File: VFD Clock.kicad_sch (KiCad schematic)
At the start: 27 parts, among them J1 DS3231, U1 74HC595, U10 74HC595, U11 UDN2981A, U12 IV-11 VFD Tube, U13 74HC595, U14 UDN2981A, U15 IV-11 VFD Tube, U16 74HC595, U17 UDN2981A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

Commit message: omg I finally figured out how to link the UDN2981A symbol and footprint I am the goat
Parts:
- added U19: XL6009 Module, Custom Parts:XL6009 Module, symbol Custom Parts:XL6009_Module
- added U20: LM2596 Module, Custom Parts:LM2596 Module, symbol Custom Parts:LM2596_module
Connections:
- net +1.5V: now also U20.3 (Out+)
- net +25V: now also U19.3 (Out+)
- net +5V: now also U19.1 (In+), U20.1 (In+)
- net GND: now also U19.2 (In-), U19.4 (Out-), U20.2 (In-), U20.4 (Out-)

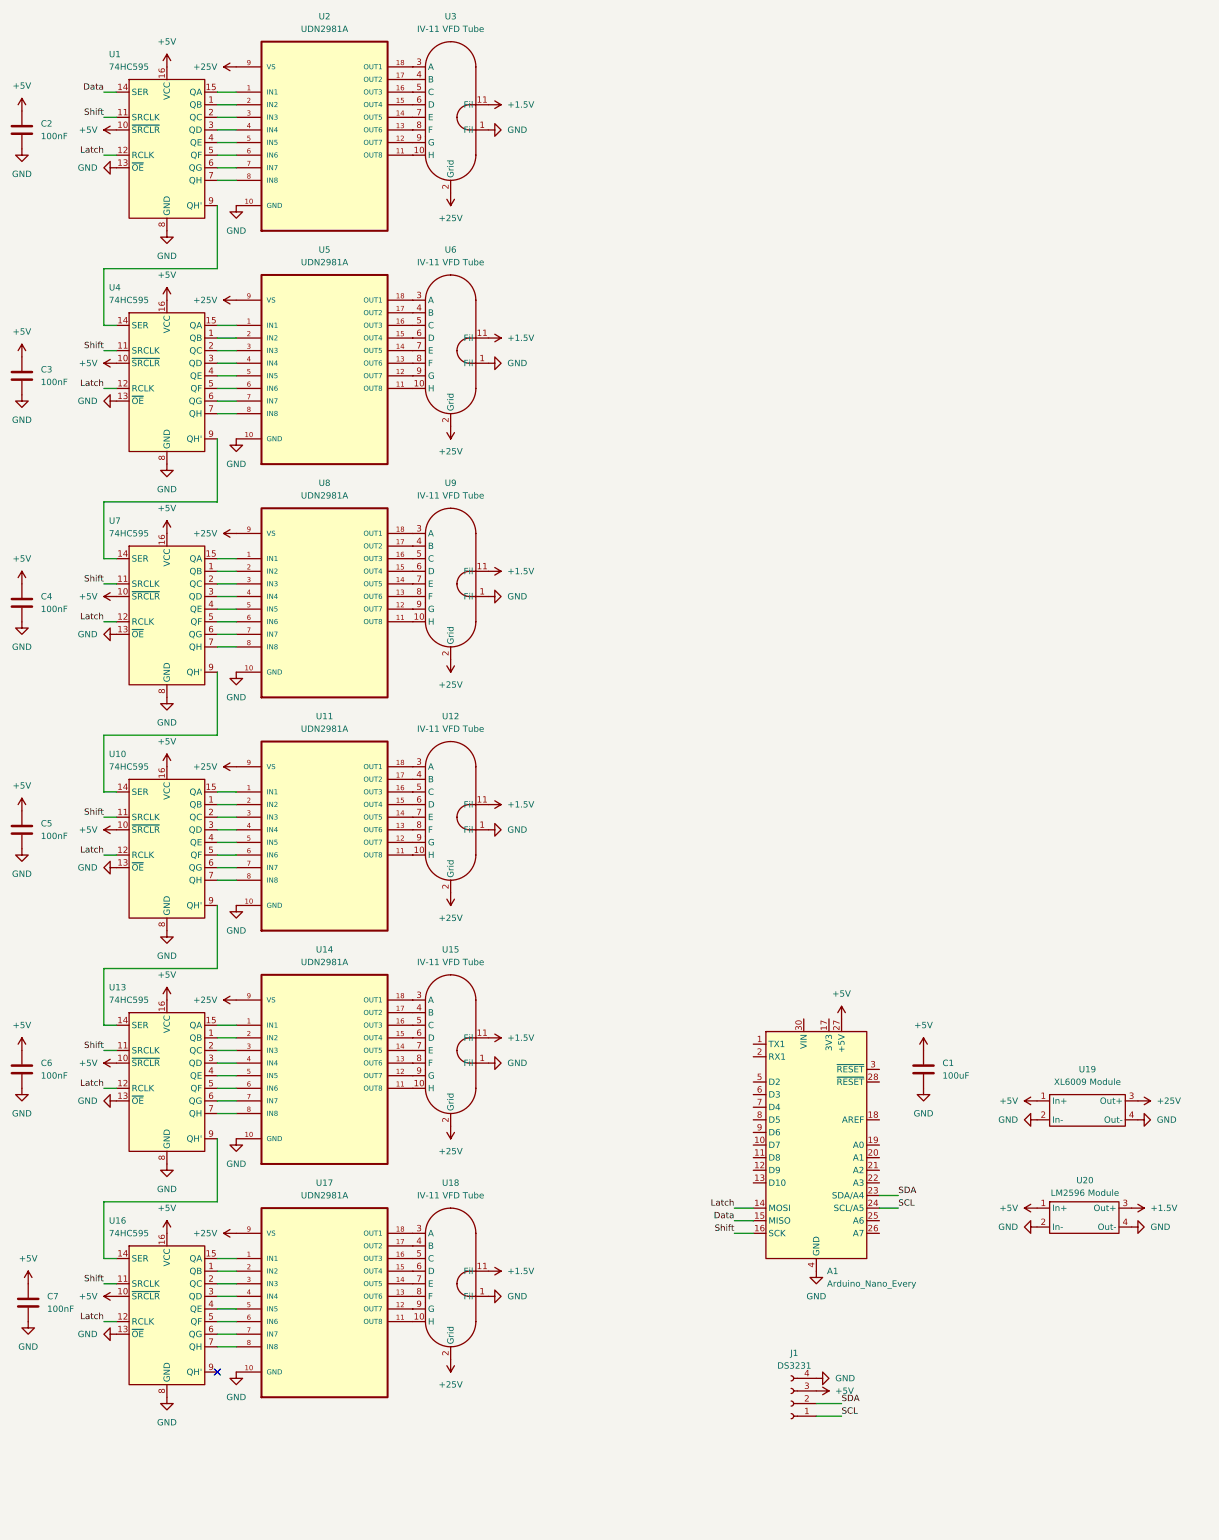
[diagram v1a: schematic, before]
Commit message: added OE PWM functionality to control the brightness of every tube using software
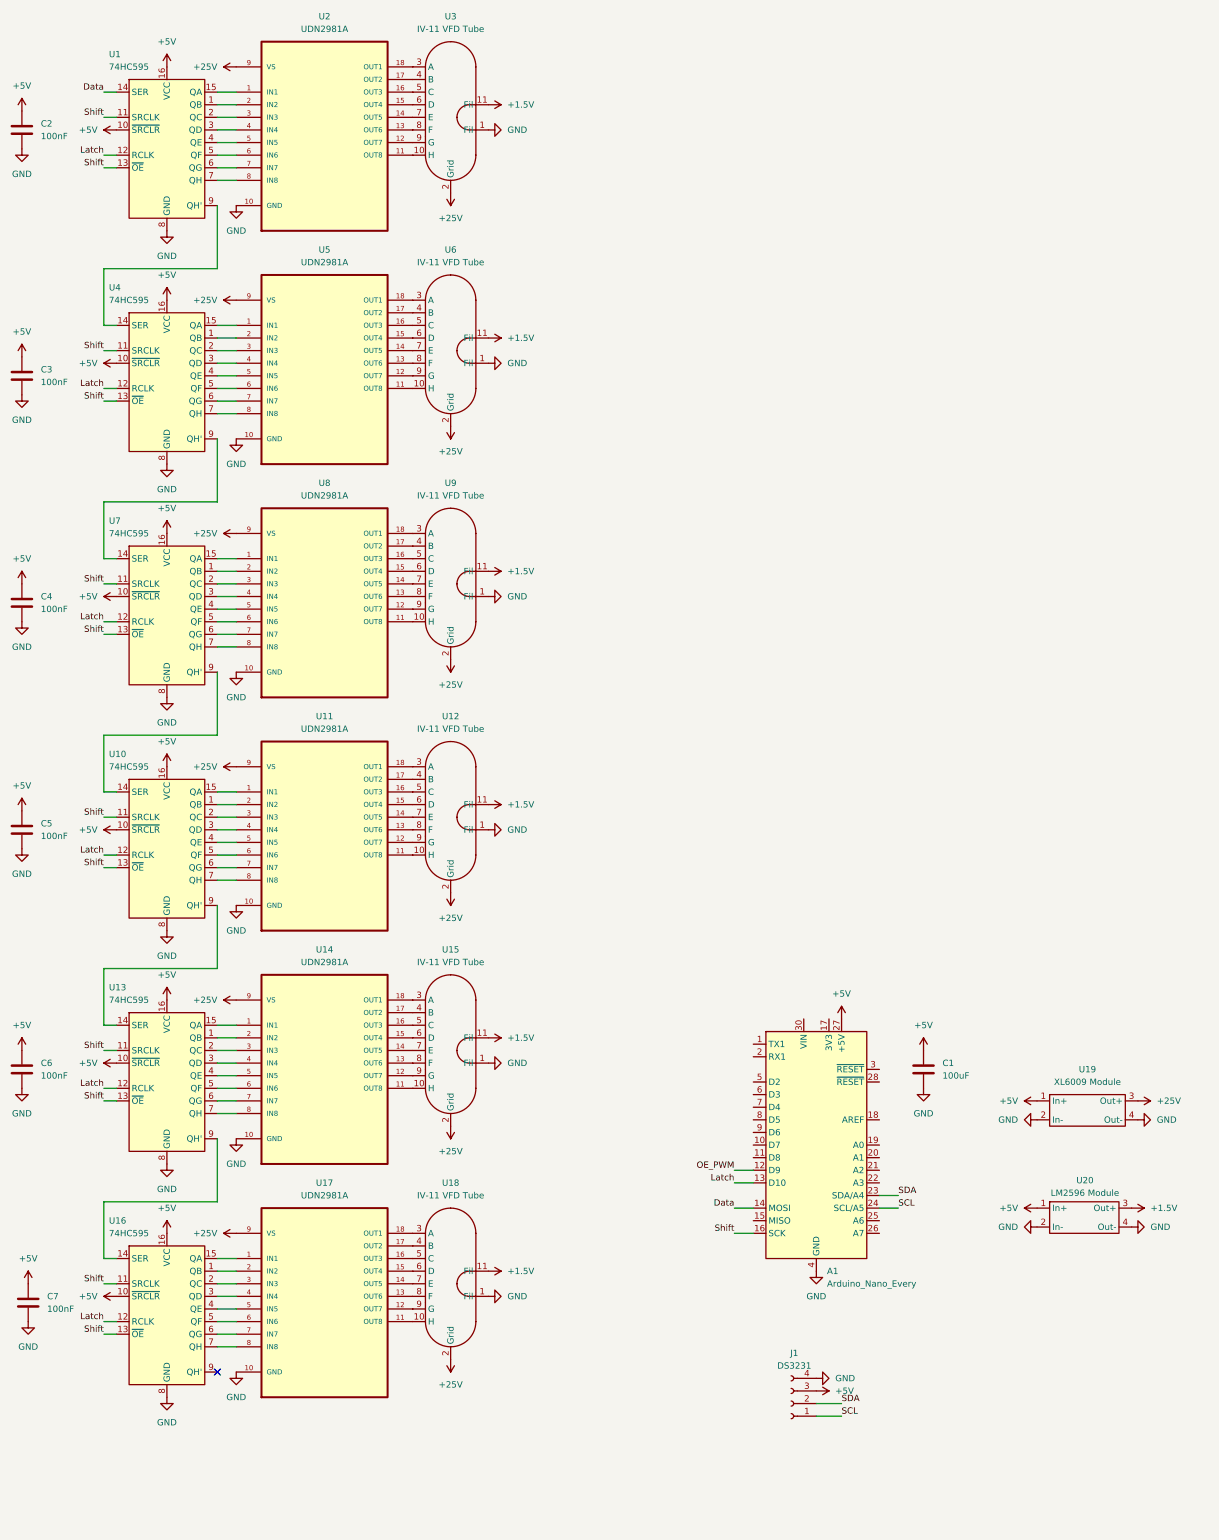
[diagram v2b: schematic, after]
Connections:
- net Data: now also A1.14 (MOSI); no longer A1.15 (MISO)
- net GND: no longer U1.13 (~{OE}), U10.13 (~{OE}), U13.13 (~{OE}), U16.13 (~{OE}), U4.13 (~{OE}), U7.13 (~{OE})
- net Latch: now also A1.13 (D10); no longer A1.14 (MOSI)
- net Shift: now also U1.13 (~{OE}), U10.13 (~{OE}), U13.13 (~{OE}), U16.13 (~{OE}), U4.13 (~{OE}), U7.13 (~{OE})
- net OE_PWM: now reaches A1.12 (D9)

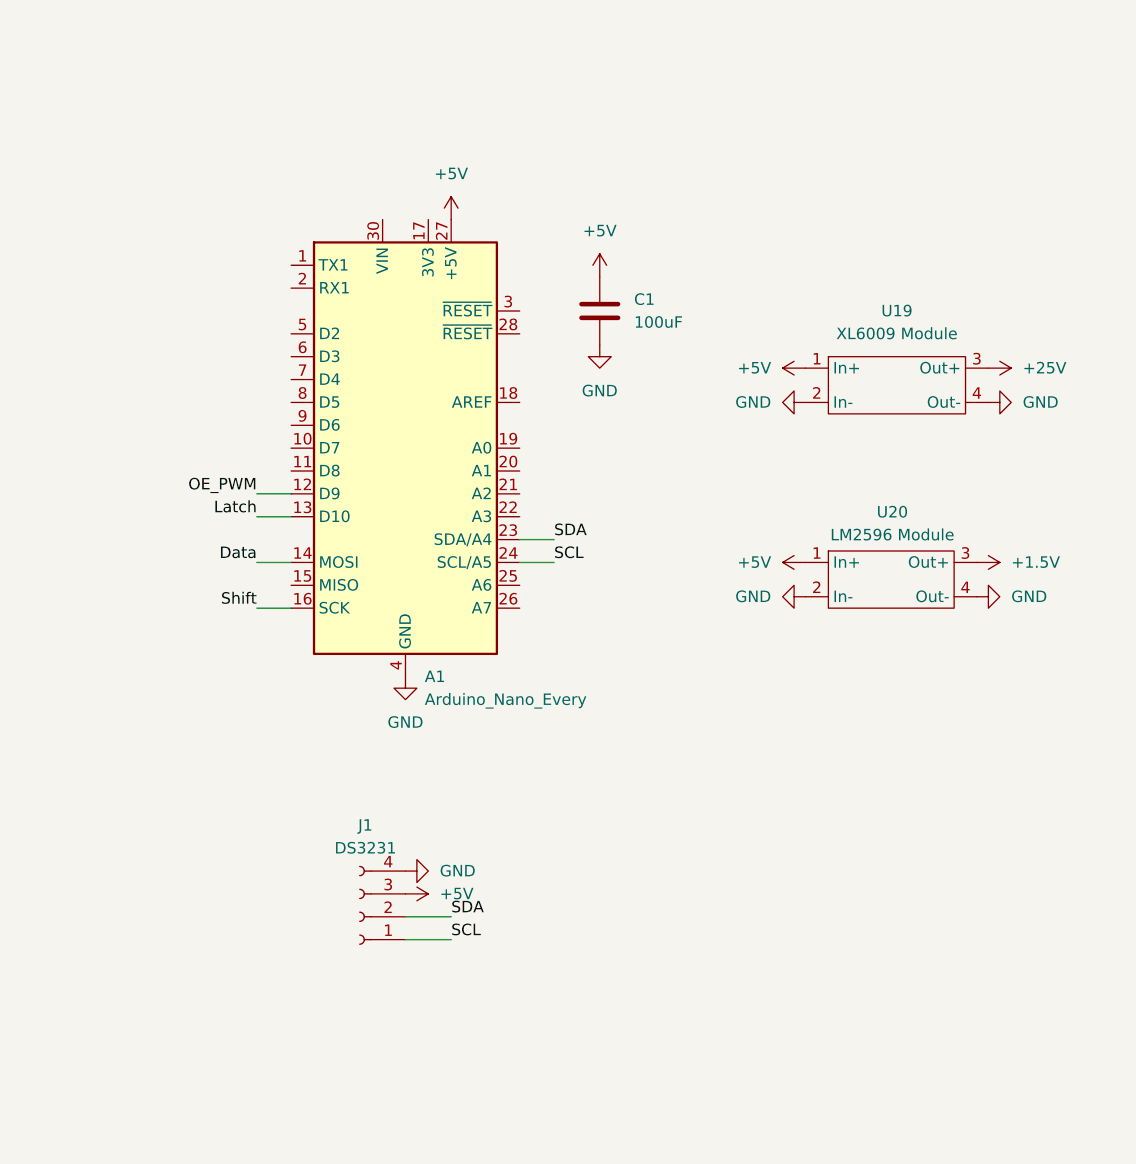
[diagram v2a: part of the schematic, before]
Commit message: added buttons, power LED, and more
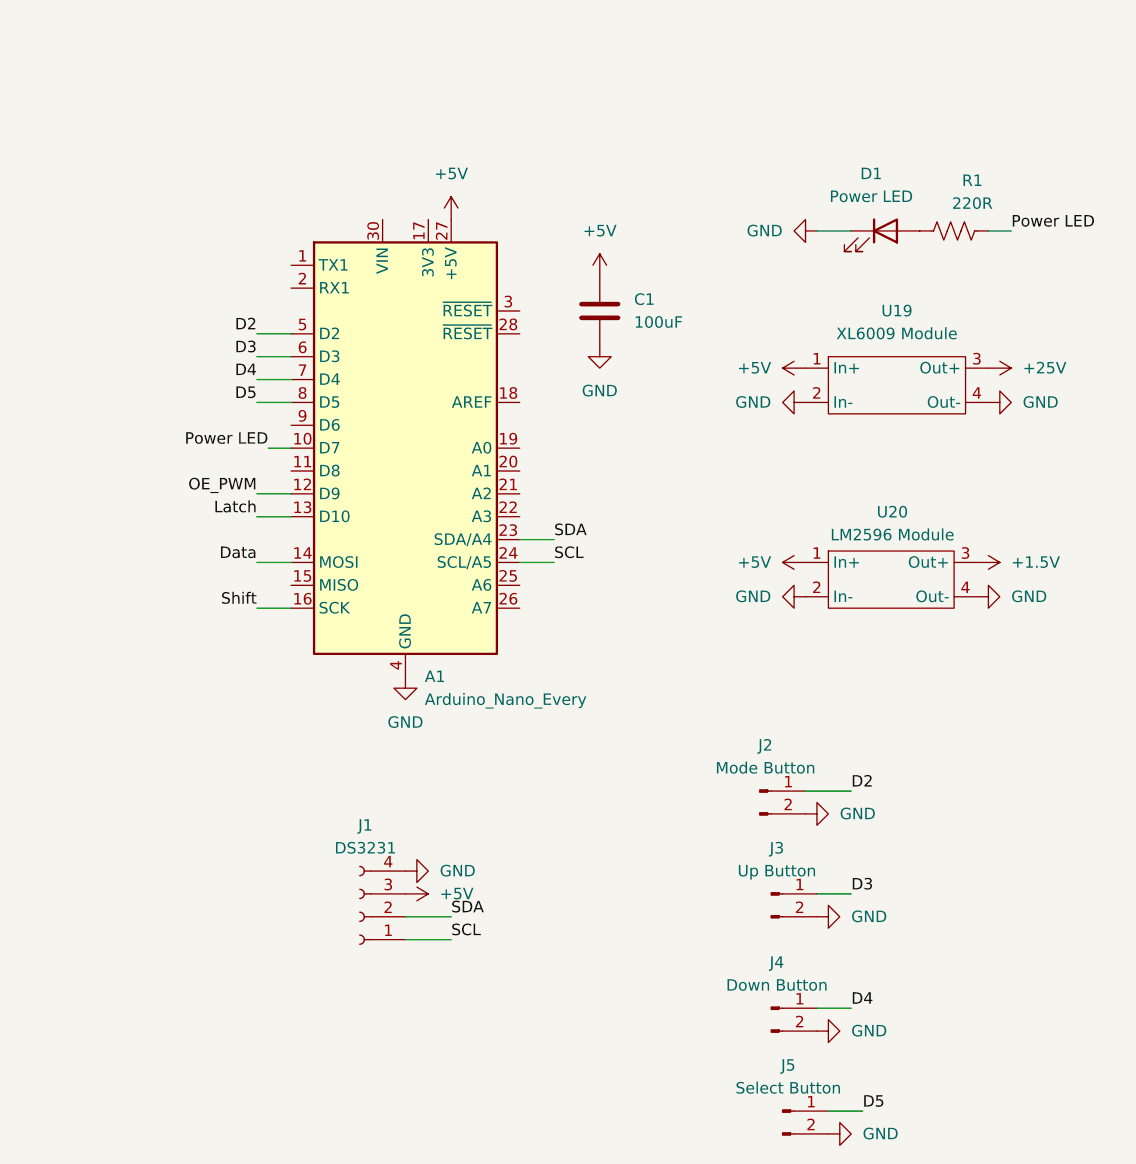
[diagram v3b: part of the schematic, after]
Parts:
- added D1: Power LED, symbol Device:LED
- added J2: Mode Button, symbol Connector:Conn_01x02_Pin
- added J3: Up Button, symbol Connector:Conn_01x02_Pin
- added J4: Down Button, symbol Connector:Conn_01x02_Pin
- added J5: Select Button, symbol Connector:Conn_01x02_Pin
- added R1: 220R, symbol Device:R_US
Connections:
- net GND: now also D1.1 (K), J2.2 (Pin_2), J3.2 (Pin_2), J4.2 (Pin_2), J5.2 (Pin_2)
- net Power LED: now reaches A1.10 (D7)
- net Power LED: now also R1.2
- net D2: now reaches A1.5 (D2)
- net D2: now also J2.1 (Pin_1)
- net D3: now reaches A1.6 (D3)
- net D3: now also J3.1 (Pin_1)
- net D4: now reaches A1.7 (D4)
- net D4: now also J4.1 (Pin_1)
- net D5: now reaches A1.8 (D5)
- net D5: now also J5.1 (Pin_1)
- new net: D1.2 (A), R1.1

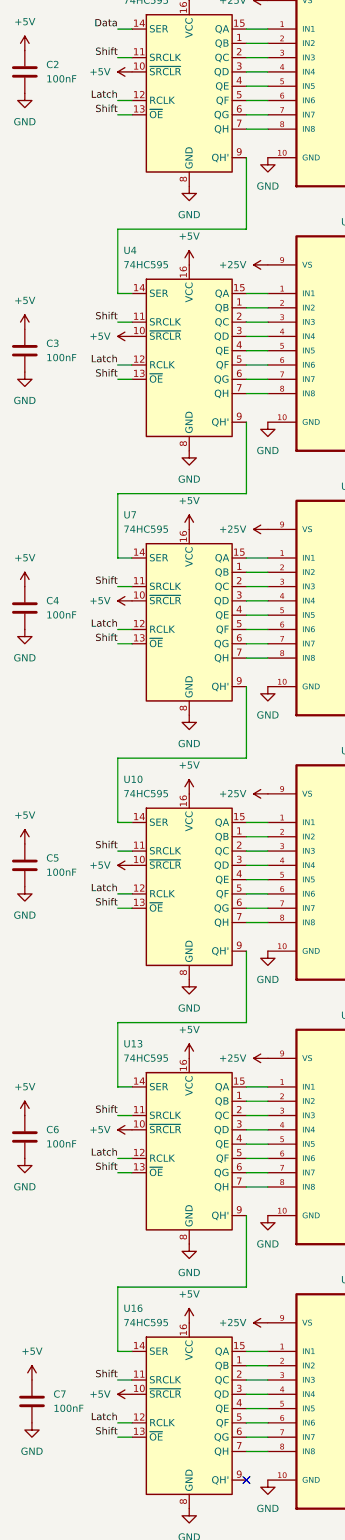
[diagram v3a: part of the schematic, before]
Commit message: added arduino code and fixed schematic bug
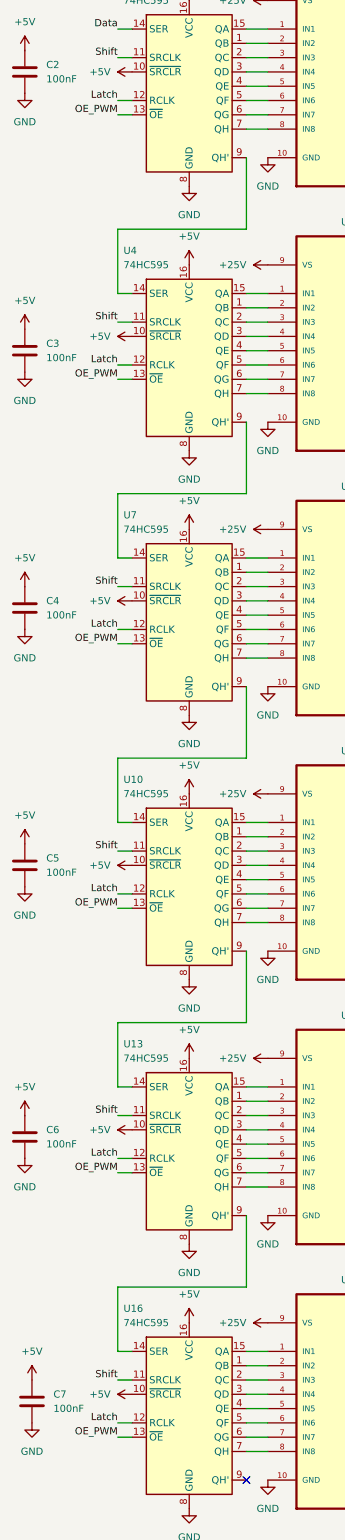
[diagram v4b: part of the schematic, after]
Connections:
- net OE_PWM: now also U1.13 (~{OE}), U10.13 (~{OE}), U13.13 (~{OE}), U16.13 (~{OE}), U4.13 (~{OE}), U7.13 (~{OE})
- net Shift: no longer U1.13 (~{OE}), U10.13 (~{OE}), U13.13 (~{OE}), U16.13 (~{OE}), U4.13 (~{OE}), U7.13 (~{OE})
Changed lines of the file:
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@@
 		)
 	)
-	(label "Shift"
+	(label "OE_PWM"
 		(at 36.83 288.29 180)
 		(effects
@@
 		)
 	)
-	(label "Shift"
+	(label "OE_PWM"
 		(at 36.83 53.34 180)
 		(effects
@@
 		)
 	)
-	(label "Shift"
+	(label "OE_PWM"
 		(at 36.83 194.31 180)
 		(effects
@@
 		)
 	)
-	(label "Shift"
+	(label "OE_PWM"
 		(at 36.83 147.32 180)
 		(effects
@@
 		)
 	)
-	(label "Shift"
+	(label "OE_PWM"
 		(at 36.83 100.33 180)
 		(effects
@@
 		)
 	)
-	(label "Shift"
+	(label "OE_PWM"
 		(at 36.83 241.3 180)
 		(effects

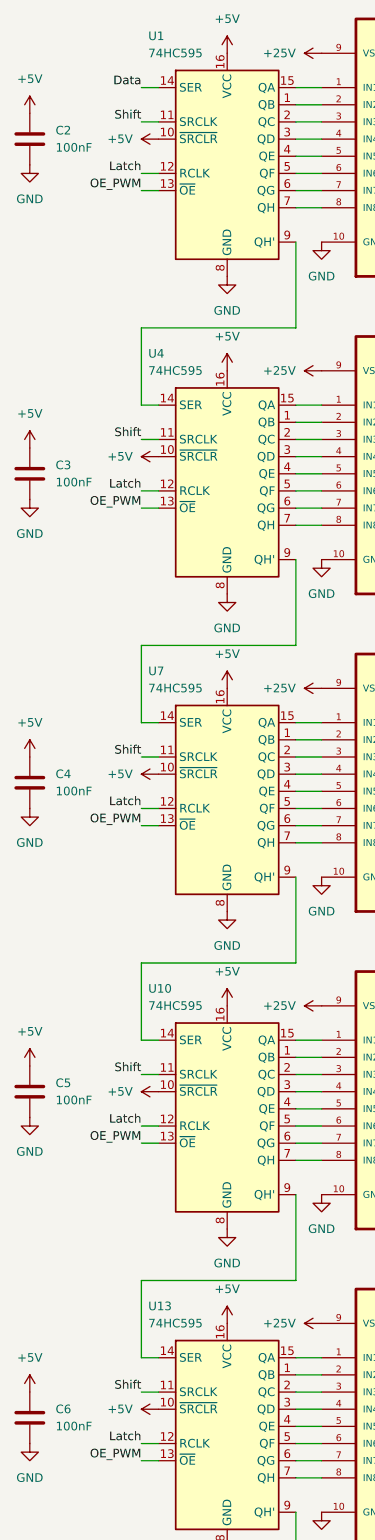
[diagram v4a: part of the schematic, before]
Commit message: started prototyping pcb layout
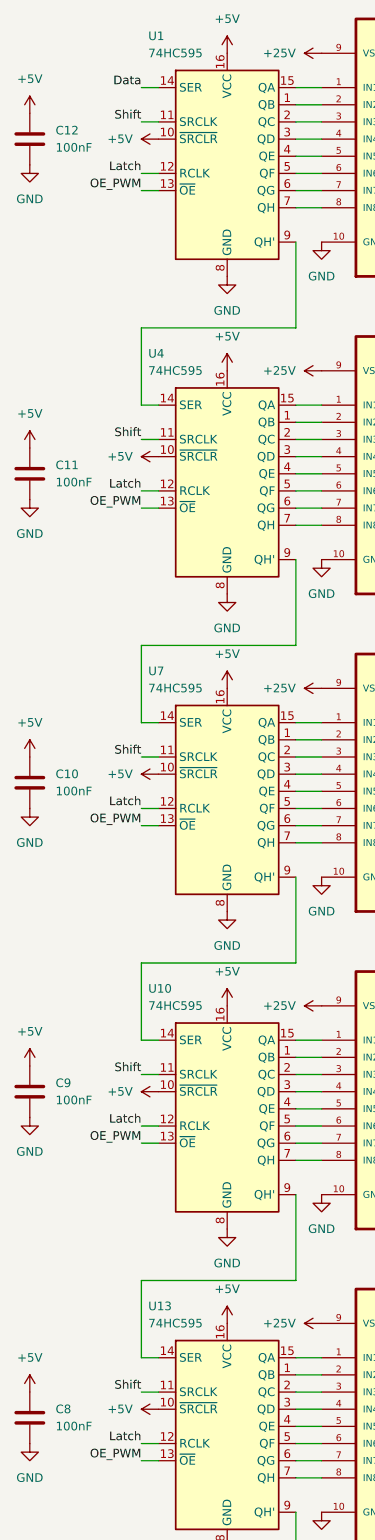
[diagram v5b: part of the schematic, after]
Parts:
- removed C2, C3, C4, C5, C6: 100nF, Capacitor_THT:CP_Radial_D6.3mm_P2.50mm, symbol Device:C
- added C10, C11, C12, C8, C9: 100nF, Capacitor_THT:C_Disc_D3.0mm_W1.6mm_P2.50mm, symbol Device:C
- C7: footprint Capacitor_THT:CP_Radial_D6.3mm_P2.50mm -> Capacitor_THT:C_Disc_D3.0mm_W1.6mm_P2.50mm
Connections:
- net +5V: now also C10.1, C11.1, C12.1, C8.1, C9.1
- net GND: now also C10.2, C11.2, C12.2, C8.2, C9.2

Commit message: schematic edit
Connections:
- net D2 renamed Mode_Button
- net D3 renamed Up_Button
- net D4 renamed Down_Button
- net D5 renamed Select_Button
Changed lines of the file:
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@@
 		)
 	)
-	(label "D2"
+	(label "Mode_Button"
 		(at 229.87 288.29 0)
 		(effects
@@
 		)
 	)
-	(label "D4"
+	(label "Down_Button"
 		(at 163.83 242.57 180)
 		(effects
@@
 		)
 	)
-	(label "D5"
+	(label "Select_Button"
 		(at 231.14 323.85 0)
 		(effects
@@
 		)
 	)
-	(label "D2"
+	(label "Mode_Button"
 		(at 163.83 237.49 180)
 		(effects
@@
 		)
 	)
-	(label "D4"
+	(label "Down_Button"
 		(at 229.87 312.42 0)
 		(effects
@@
 		)
 	)
-	(label "D3"
+	(label "Up_Button"
 		(at 163.83 240.03 180)
 		(effects
@@
 		)
 	)
-	(label "D5"
+	(label "Select_Button"
 		(at 163.83 245.11 180)
 		(effects
@@
 		)
 	)
-	(label "D3"
+	(label "Up_Button"
 		(at 229.87 299.72 0)
 		(effects
